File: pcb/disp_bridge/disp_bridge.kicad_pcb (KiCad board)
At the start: 2 copper layers, 40 x 70 mm, 5 parts, among them J1 CONN_01X21, J2 CONN_01X21, J3 CONN_01X21, J4 CONN_02X13, J5 CONN_02X13

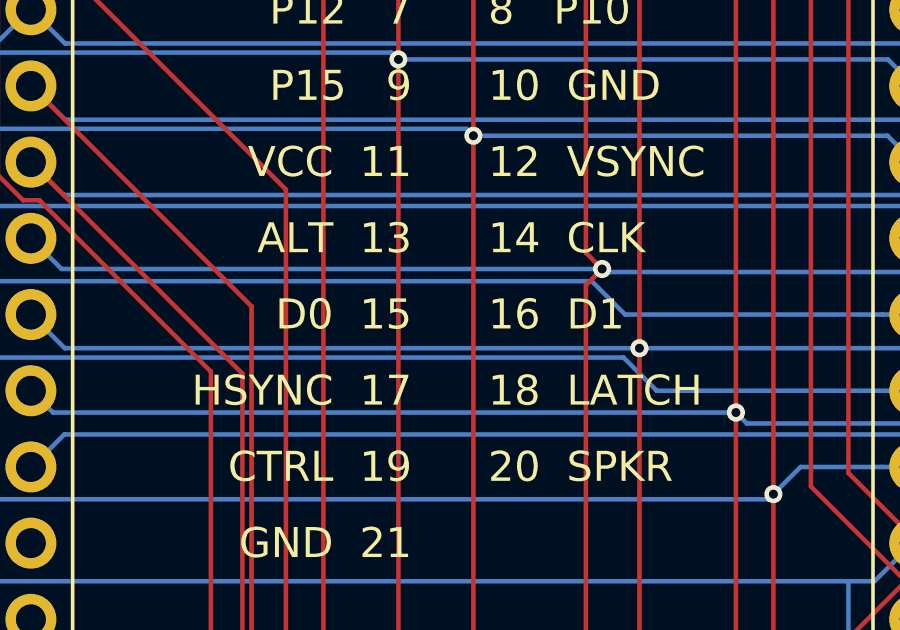
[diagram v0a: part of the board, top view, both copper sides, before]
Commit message: fix labeling of D0&D1 LCD signals
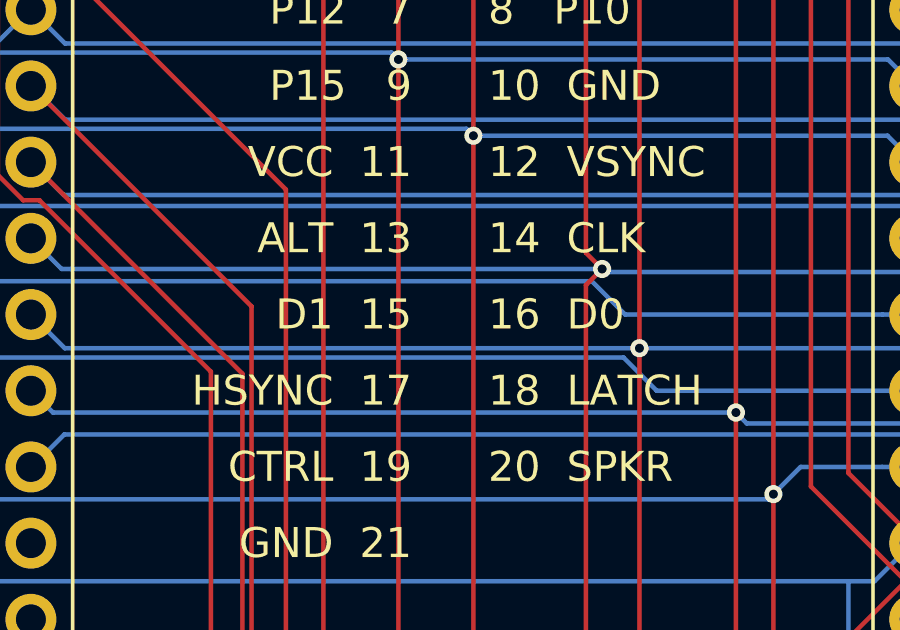
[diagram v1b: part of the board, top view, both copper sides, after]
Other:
- board text added: "16 D0"
- board text added: "D1 15"
- board text removed: "16 D1"
- board text removed: "D0 15"
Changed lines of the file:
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@@
   (title_block
     (title "Display Bridge")
-    (date 2019-08-10)
-    (rev 0)
+    (date 2019-10-06)
+    (rev 1)
     (company "Author: Michael Singer")
     (comment 1 https://sourceforge.net/projects/iceboy/)
@@
     (effects (font (size 1 1) (thickness 0.15)) (justify left))
   )
-  (gr_text "16  D1" (at 160.24 92.7) (layer F.SilkS)
+  (gr_text "16  D0" (at 160.24 92.7) (layer F.SilkS)
     (effects (font (size 1 1) (thickness 0.15)) (justify left))
   )
@@
     (effects (font (size 1 1) (thickness 0.15)) (justify right))
   )
-  (gr_text "D0  15" (at 157.7 92.7) (layer F.SilkS)
+  (gr_text "D1  15" (at 157.7 92.7) (layer F.SilkS)
     (effects (font (size 1 1) (thickness 0.15)) (justify right))
   )

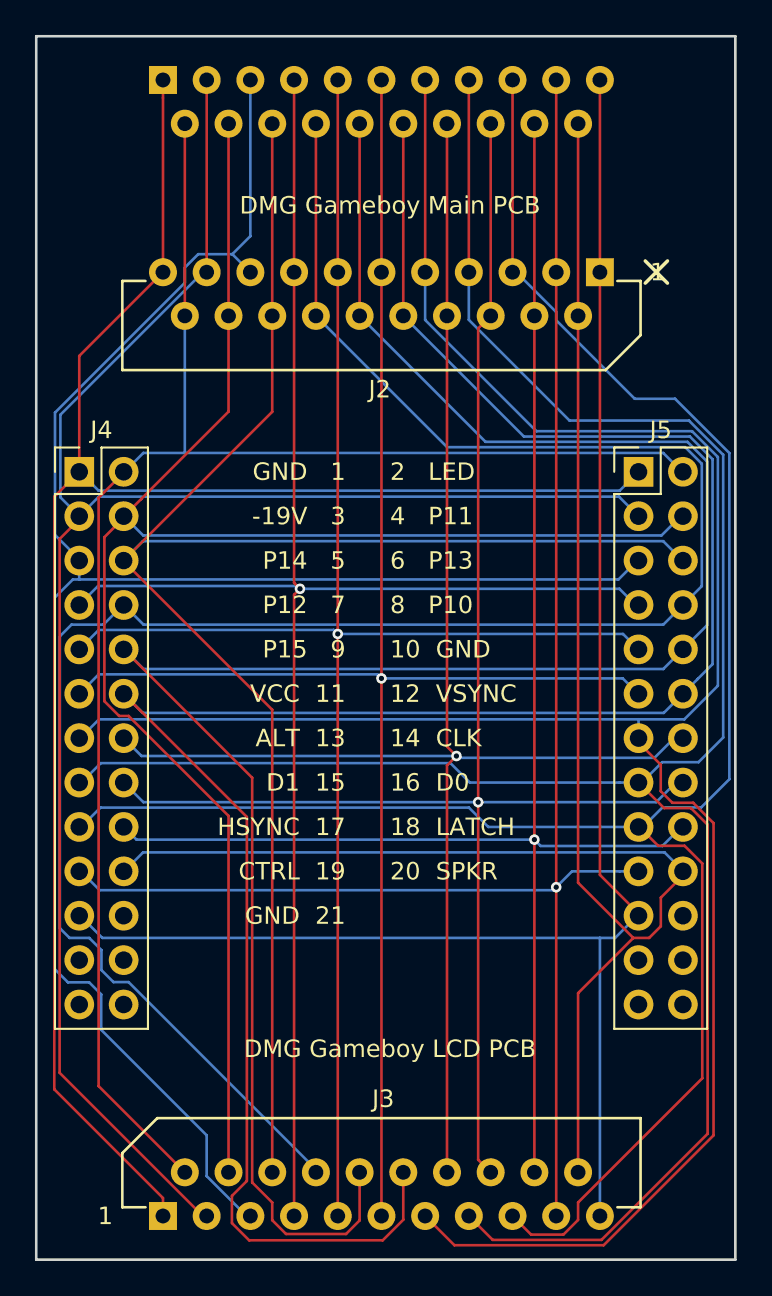
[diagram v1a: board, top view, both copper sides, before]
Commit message: Migrate other PCBs from KiCad 4 to KiCad 8
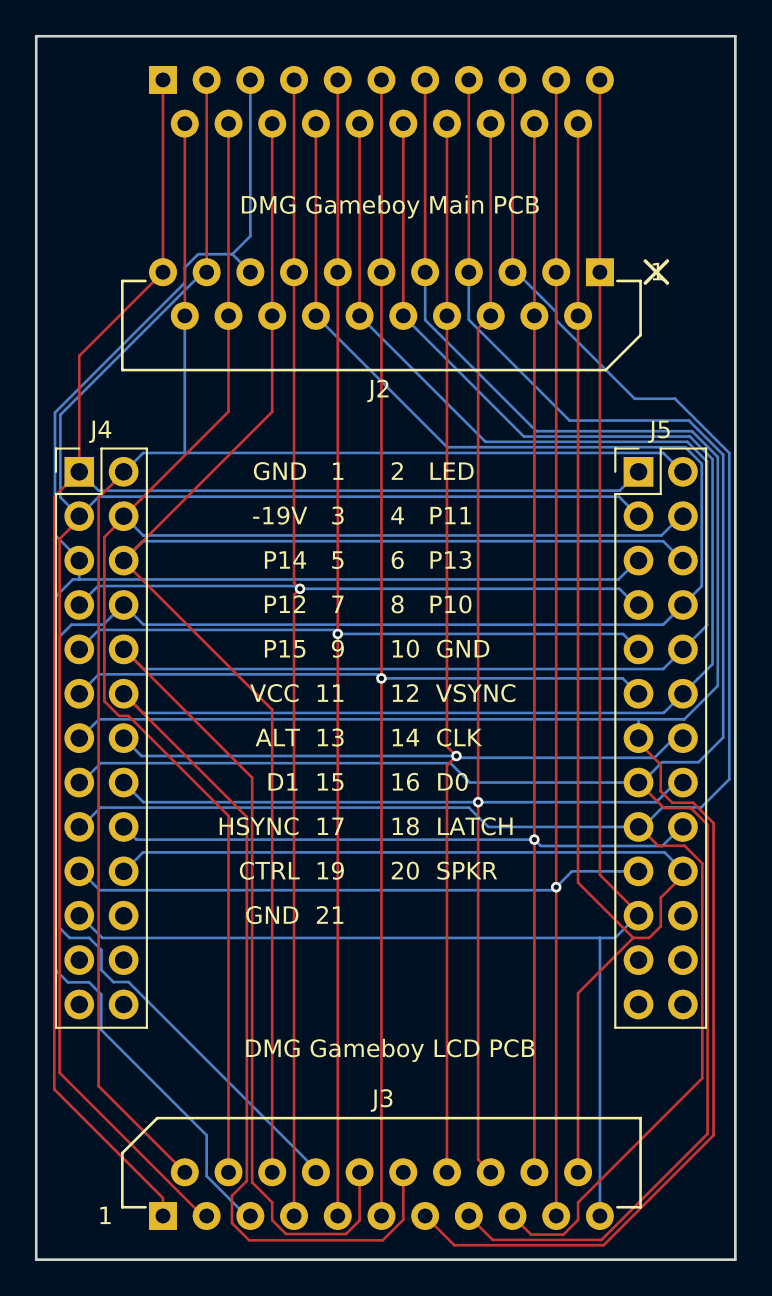
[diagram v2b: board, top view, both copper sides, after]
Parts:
- J1, J2, J3: value CONN_01X21 -> Conn_01x21; footprint fcc:Molex-SD-52045-2145 -> Connector_GameBoy:DMG_FFC_LCD-Board_21Pin
- J4, J5: value CONN_02X13 -> Conn_02x13_Odd_Even; footprint Pin_Headers:Pin_Header_Straight_2x13_Pitch2.54mm -> Connector_PinHeader_2.54mm:PinHeader_2x13_P2.54mm_Vertical
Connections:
- J4 pad 22: Net-(J4-Pad22) -> unconnected-(J4-Pin_22-Pad22)
- J4 pad 23: Net-(J4-Pad23) -> unconnected-(J4-Pin_23-Pad23)
- J4 pad 24: Net-(J4-Pad24) -> unconnected-(J4-Pin_24-Pad24)
- J4 pad 25: Net-(J4-Pad25) -> unconnected-(J4-Pin_25-Pad25)
- J4 pad 26: Net-(J4-Pad26) -> unconnected-(J4-Pin_26-Pad26)
- J5 pad 22: Net-(J5-Pad22) -> unconnected-(J5-Pin_22-Pad22)
- J5 pad 23: Net-(J5-Pad23) -> unconnected-(J5-Pin_23-Pad23)
- J5 pad 24: Net-(J5-Pad24) -> unconnected-(J5-Pin_24-Pad24)
- J5 pad 25: Net-(J5-Pad25) -> unconnected-(J5-Pin_25-Pad25)
- J5 pad 26: Net-(J5-Pad26) -> unconnected-(J5-Pin_26-Pad26)
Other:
- net class Default removed
